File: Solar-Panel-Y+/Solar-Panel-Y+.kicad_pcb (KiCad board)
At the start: 6 copper layers, 50 x 50 mm, 81 parts, among them J1 FTS-105-01-L-DV-A, Q1 BSS138DWQ-7, Q2 MBT2222ADW1T1, Q3 BSS138DWQ-7, Q4 MBT2222ADW1T1, U1 Value, U2 TSL2561

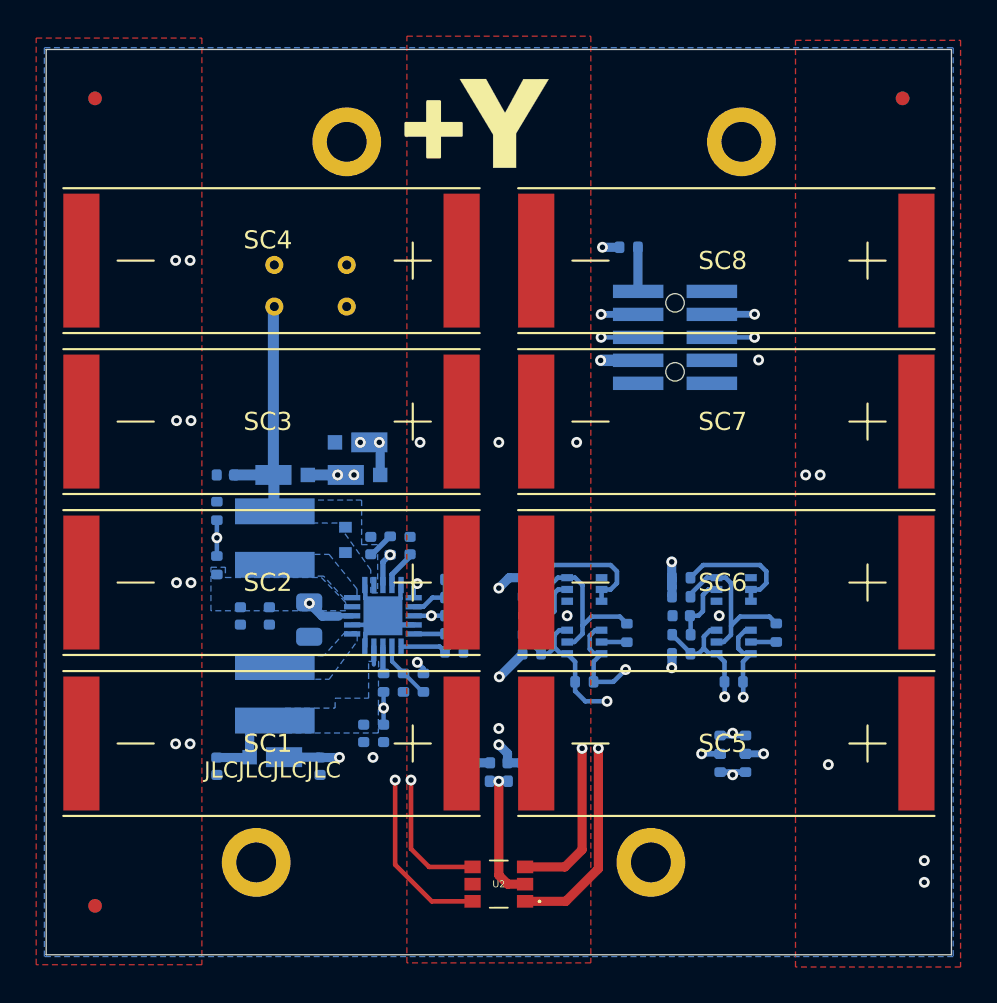
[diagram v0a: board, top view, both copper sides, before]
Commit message: Finish 6 Layer panel versions
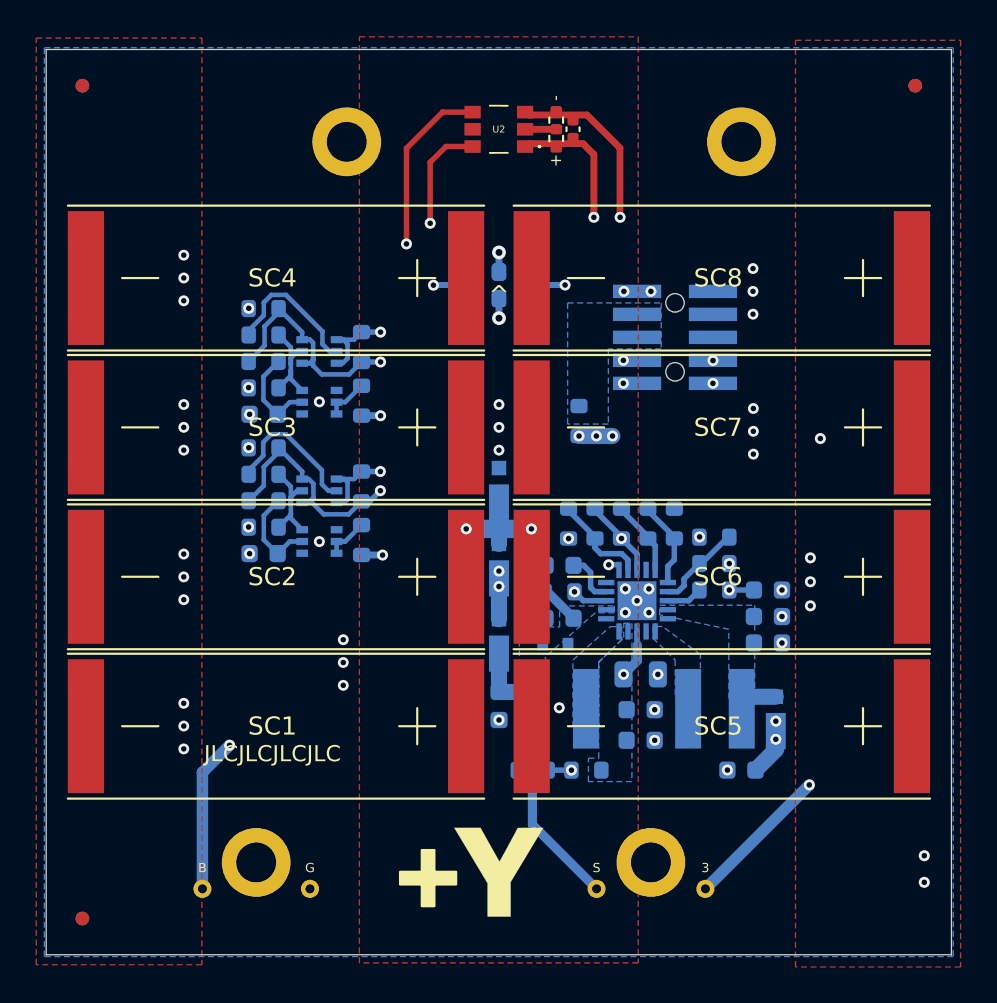
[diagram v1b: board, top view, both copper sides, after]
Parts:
- removed the Ref** at (95.2, 78.9)
- added Ref**: Val**, custom-footprints:pycubed_mini_half, B.Cu at (104.6, 39.3)
- C1, R1, R2: moved to F.Cu
- C10, C11, C12, C13, C2, C3, C4, C6, C7, C8, C9: footprint Capacitor_SMD:C_0402_1005Metric -> Capacitor_SMD:C_0603_1608Metric
- J1: footprint batteryboard:FTS-105-XX-YY-DV-A -> solarpanels:SAMTEC-FTS-105-01-X-DV-A
- R10, R11, R12, R13, R16, R17, R18, R3, R5, R6, R7, R8, R9: footprint Resistor_SMD:R_0402_1005Metric -> Resistor_SMD:R_0603_1608Metric
- R14, R15: value 0 -> DNI; footprint Resistor_SMD:R_0402_1005Metric -> Resistor_SMD:R_0603_1608Metric
- R19: renamed from R22; value 0 -> DNI; footprint Resistor_SMD:R_0402_1005Metric -> Resistor_SMD:R_0603_1608Metric
- R20: renamed from R23; value 0 -> DNI; footprint Resistor_SMD:R_0402_1005Metric -> Resistor_SMD:R_0603_1608Metric
- R21: renamed from R20; footprint Resistor_SMD:R_0402_1005Metric -> Resistor_SMD:R_0603_1608Metric
- R22: renamed from R21; footprint Resistor_SMD:R_0402_1005Metric -> Resistor_SMD:R_0603_1608Metric
- R23: renamed from R24; footprint Resistor_SMD:R_0402_1005Metric -> Resistor_SMD:R_0603_1608Metric
- R24: renamed from R25; footprint Resistor_SMD:R_0402_1005Metric -> Resistor_SMD:R_0603_1608Metric
- R25: renamed from R26; footprint Resistor_SMD:R_0402_1005Metric -> Resistor_SMD:R_0603_1608Metric
- R26: renamed from R27; footprint Resistor_SMD:R_0402_1005Metric -> Resistor_SMD:R_0603_1608Metric
- R27: renamed from R28; footprint Resistor_SMD:R_0402_1005Metric -> Resistor_SMD:R_0603_1608Metric
- R28: renamed from R29; footprint Resistor_SMD:R_0402_1005Metric -> Resistor_SMD:R_0603_1608Metric
- R29: renamed from R30; footprint Resistor_SMD:R_0402_1005Metric -> Resistor_SMD:R_0603_1608Metric
- R30: renamed from R31; footprint Resistor_SMD:R_0402_1005Metric -> Resistor_SMD:R_0603_1608Metric
- R4: renamed from R19; footprint Resistor_SMD:R_0402_1005Metric -> Resistor_SMD:R_0603_1608Metric
- moved U2 41.7 mm to (104.6, 39.6)
- moved Ref** 41.4 mm to (121.6, 81.6)
- moved TP3 37.8 mm to (116.0, 81.6)
- moved TP1 36.8 mm to (110.0, 81.6)
- moved R2 36.8 mm to (107.8, 39.1), turned to 90 degrees
- moved R1 35.6 mm to (107.8, 40.1), turned to 90 degrees
- moved TP4 35.4 mm to (88.2, 81.6)
- moved C1 35.2 mm to (108.7, 39.6), turned to 90 degrees
- moved TP2 34.5 mm to (94.2, 81.6)
- moved R21 32.7 mm to (91.6, 51.0), turned to 0 degrees
- moved C10 31.2 mm to (119.5, 68.0), turned to 0 degrees
- moved R17 30.0 mm to (105.4, 47.5), turned to 180 degrees
- moved R24 29.9 mm to (91.6, 49.5)
- moved R18 29.8 mm to (103.8, 47.5), turned to 180 degrees
- moved R12 28.1 mm to (105.4, 49.0), turned to 180 degrees
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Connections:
- net Net-(D4-Pad1) renamed /VSOLAR_FULL
- J1 pad 1: unconnected-(J1-Pad1) -> GND
- J1 pad 10: VBUS -> SDA
- J1 pad 2: unconnected-(J1-Pad2) -> +3V3
- J1 pad 3: +3V3 -> GND
- J1 pad 4: GND -> BATT_P
- J1 pad 5: SDA3 -> unconnected-(J1-Pad5)
- J1 pad 6: SCL3 -> BATT_P
- J1 pad 7: COIL_P -> COIL_N
- J1 pad 8: COIL_N -> SCL
- J1 pad 9: BATT_P -> COIL_P
- Q2 pad 1: SCL3 -> SCL
- Q2 pad 3: SCL3 -> SCL
- Q4 pad 1: SDA3 -> SDA
- Q4 pad 3: SDA3 -> SDA
- R19 pad 2: SCL3 -> SCL
- R20 pad 2: SDA3 -> SDA
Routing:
- net /coil: track 12252.9 -> 12568.6 mm
- net VBAT: track 44.3 -> 13.1 mm, vias 2 -> 5
- net SCL3: track 27.3 -> 0.00 mm, vias 2 -> 0
- net SDA3: track 27.0 -> 0.00 mm, vias 2 -> 0
- net SDA: track 0.00 -> 21.6 mm, vias 0 -> 2
- net SCL: track 0.00 -> 18.9 mm, vias 0 -> 2
- net COIL_P: track 29.6 -> 14.4 mm
- net COIL_N: track 28.8 -> 16.8 mm
- net GND: track 17.9 -> 9.67 mm, vias 14 -> 45
- net +3V3: track 27.3 -> 19.9 mm, vias 8 -> 12
- net Net-(D3-Pad1): track 13.1 -> 5.89 mm, vias 5 -> 2
- net Net-(Q4-Pad2): track 1.39 -> 7.86 mm
- net Net-(Q2-Pad2): track 1.40 -> 7.79 mm
- net Net-(R1-Pad2): track 7.86 -> 1.72 mm, vias 1 -> 0
- net SCL_LS: track 34.6 -> 29.7 mm
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- added copper zone on In3.Cu, net +3V3
- added copper zone on B.Cu, net BATT_P
- added copper zone on In1.Cu, net GND
- added copper zone on In2.Cu, net VBAT
- removed copper zone on In1.Cu, net +3V3
- removed copper zone on In2.Cu, net +3V3
- removed copper zone on In3.Cu, net GND
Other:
- board text added: "1.GND 3.GND 5.NC 7.COIL_N 9.COIL_P"
- board text added: "2.3V3 4.BATT_P 6.BATT_P 8.SCL 10.SDA"
- board text added: "3"
- board text added: "B"
- board text added: "G"
- board text added: "Rev B2/01"
- board text added: "S"
- board text added: "^"
- board text added: "⊗"
- board text added: "⊙"
- board text removed: "Cable Pinout 1.BATT_P 2.VUSB 3.BURN1 4.BURN2 5.COIL_P 6.COIL_N 7.SDA 8.SCL 9.+3V3 10.GND"
- board text removed: "v04"
